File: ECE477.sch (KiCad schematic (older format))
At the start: 55 parts, among them IC1 LP3852EMP-3.3_NOPB, IC2 BQ29330DBT, J1 P7805-2000-S, J2 Conn_01x05_Male, J3 Conn_01x05_Male, J4 Conn_01x05_Male, J5 Conn_01x05_Male, J6 Conn_01x05_Male, SW1 SW_Push_Dual, U1 STM32H7_LQFP144_T2

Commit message: Updated Bat monitor
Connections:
- net GND: now also IC2.23 (VSS_2), IC2.4 (VSS_1); no longer IC2.1 (CELL-)
- net PWR_IN: now also IC2.19 (VCC); no longer IC2.2 (CELL+)
- net LED_PWR: now reaches IC2.24 (LEDOUT)
- net CLK: now reaches IC2.26 (WDI)
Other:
- moved on the sheet: IC2
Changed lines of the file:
@@
 Touch_Input
 Wire Wire Line
-	16100 2000 16450 2000
-Wire Wire Line
-	16100 2100 16450 2100
-Wire Wire Line
-	16100 2200 16450 2200
-Text GLabel 16450 2000 2    50   Input ~ 0
+	16650 2000 17000 2000
+Wire Wire Line
+	16650 2100 17000 2100
+Wire Wire Line
+	16650 2200 17000 2200
+Text GLabel 17000 2000 2    50   Input ~ 0
 I2C2_SMBA
-Text GLabel 16450 2100 2    50   Input ~ 0
+Text GLabel 17000 2100 2    50   Input ~ 0
 I2C2_SDA
-Text GLabel 16450 2200 2    50   Input ~ 0
+Text GLabel 17000 2200 2    50   Input ~ 0
 I2C2_SCL
 $Comp
 L ECE477-rescue:BQ29330DBT-SamacSys_Parts IC2
 U 1 1 5F7B6D95
-P 14800 2000
-F 0 "IC2" H 15450 2265 50  0000 C CNN
-F 1 "BQ29330DBT" H 15450 2174 50  0000 C CNN
-F 2 "SamacSys_Parts:SOP50P640X120-30N" H 25950 4500 50  0001 L CNN
-F 3 "http://www.ti.com/general/docs/suppproductinfo.tsp?distId=26&gotoUrl=http%3A%2F%2Fwww.ti.com%2Flit%2Fgpn%2Fbq29330" H 25950 4400 50  0001 L CNN
-F 4 "TEXAS INSTRUMENTS - BQ29330DBT. - Li-Ion Battery, Li-Pol Full Protector, 2/3/4 Series, I2C interface, 4.5 V to 28 V supply, TSSOP-30" H 25950 4300 50  0001 L CNN "Description"
-F 5 "1.2" H 25950 4200 50  0001 L CNN "Height"
-F 6 "595-BQ29330DBT" H 25950 4100 50  0001 L CNN "Mouser Part Number"
-F 7 "https://www.mouser.co.uk/ProductDetail/Texas-Instruments/BQ29330DBT?qs=YxwvVplHM%2FnxR6WOWVPfQQ%3D%3D" H 25950 4000 50  0001 L CNN "Mouser Price/Stock"
-F 8 "Texas Instruments" H 25950 3900 50  0001 L CNN "Manufacturer_Name"
-F 9 "BQ29330DBT" H 25950 3800 50  0001 L CNN "Manufacturer_Part_Number"
-	1    14800 2000
+P 15350 2000
+F 0 "IC2" H 16000 2265 50  0000 C CNN
+F 1 "BQ29330DBT" H 16000 2174 50  0000 C CNN
+F 2 "SamacSys_Parts:SOP50P640X120-30N" H 26500 4500 50  0001 L CNN
+F 3 "http://www.ti.com/general/docs/suppproductinfo.tsp?distId=26&gotoUrl=http%3A%2F%2Fwww.ti.com%2Flit%2Fgpn%2Fbq29330" H 26500 4400 50  0001 L CNN
+F 4 "TEXAS INSTRUMENTS - BQ29330DBT. - Li-Ion Battery, Li-Pol Full Protector, 2/3/4 Series, I2C interface, 4.5 V to 28 V supply, TSSOP-30" H 26500 4300 50  0001 L CNN "Description"
+F 5 "1.2" H 26500 4200 50  0001 L CNN "Height"
+F 6 "595-BQ29330DBT" H 26500 4100 50  0001 L CNN "Mouser Part Number"
+F 7 "https://www.mouser.co.uk/ProductDetail/Texas-Instruments/BQ29330DBT?qs=YxwvVplHM%2FnxR6WOWVPfQQ%3D%3D" H 26500 4000 50  0001 L CNN "Mouser Price/Stock"
+F 8 "Texas Instruments" H 26500 3900 50  0001 L CNN "Manufacturer_Name"
+F 9 "BQ29330DBT" H 26500 3800 50  0001 L CNN "Manufacturer_Part_Number"
+	1    15350 2000
 	1    0    0    -1
 $EndComp
@@
 Text GLabel 9700 3300 2    50   Input ~ 0
 PWM5
-Wire Wire Line
-	14800 2000 14500 2000
-Wire Wire Line
-	14800 2100 14500 2100
-Text GLabel 14500 2000 0    50   Input ~ 0
-GND
-Text GLabel 14500 2100 0    50   Input ~ 0
+Text GLabel 17000 3100 2    50   Input ~ 0
 PWR_IN
 Wire Wire Line
-	14800 3100 14450 3100
-Wire Wire Line
-	14800 3000 14450 3000
-Wire Wire Line
-	14800 2900 14450 2900
-Wire Wire Line
-	14800 2800 14450 2800
-Wire Wire Line
-	14800 2700 14450 2700
-Text GLabel 14450 2700 0    50   Input ~ 0
+	15350 3100 15000 3100
+Wire Wire Line
+	15350 3000 15000 3000
+Wire Wire Line
+	15350 2900 15000 2900
+Wire Wire Line
+	15350 2800 15000 2800
+Wire Wire Line
+	15350 2700 15000 2700
+Text GLabel 15000 2700 0    50   Input ~ 0
 V5
-Text GLabel 14450 2800 0    50   Input ~ 0
+Text GLabel 15000 2800 0    50   Input ~ 0
 V4
-Text GLabel 14450 2900 0    50   Input ~ 0
+Text GLabel 15000 2900 0    50   Input ~ 0
 V3
-Text GLabel 14450 3000 0    50   Input ~ 0
+Text GLabel 15000 3000 0    50   Input ~ 0
 V2
-Text GLabel 14450 3100 0    50   Input ~ 0
+Text GLabel 15000 3100 0    50   Input ~ 0
 V1
 Wire Notes Line
@@
 Text Notes 14800 4050 0    50   ~ 0
 review data sheet for PACK and BAT pions\n
-Wire Wire Line
-	16100 3300 16400 3300
-Text GLabel 16400 3300 2    50   Input ~ 0
+Text GLabel 17000 3300 2    50   Input ~ 0
 PWR_IN
-Wire Wire Line
-	14800 3200 14500 3200
-Text GLabel 14500 3200 0    50   Input ~ 0
+Text GLabel 15000 3200 0    50   Input ~ 0
 PWR_IN
+Wire Wire Line
+	15350 2300 15000 2300
+Wire Wire Line
+	16650 2700 17000 2700
+Wire Wire Line
+	15000 2100 15350 2100
+Wire Wire Line
+	15000 2000 15350 2000
+Text GLabel 15000 2300 0    50   Input ~ 0
+GND
+Text GLabel 17000 2700 2    50   Input ~ 0
+GND
+Wire Wire Line
+	16650 3100 17000 3100
+Wire Wire Line
+	16650 3300 17000 3300
+Wire Wire Line
+	15000 3200 15350 3200
+Wire Wire Line
+	16650 2600 17000 2600
+Text GLabel 17000 2600 2    50   Input ~ 0
+LED_PWR
+Wire Wire Line
+	16650 2400 17000 2400
+Text GLabel 17000 2400 2    50   Input ~ 0
+CLK
 $EndSCHEMATC

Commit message: Working with Routing
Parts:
- removed R5: 0R, Resistor_SMD:R_0805_2012Metric_Pad1.15x1.40mm_HandSolder, symbol Device:R_US
- added J7: Conn_01x05_Male, Connector_PinHeader_1.00mm:PinHeader_1x05_P1.00mm_Vertical, symbol Connector:Conn_01x05_Male
- added R10, R7, R8, R9: 0R, Resistor_SMD:R_0805_2012Metric_Pad1.15x1.40mm_HandSolder, symbol Device:R_US
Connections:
- net CLK is gone; now on net NC: IC2.26 (WDI)
- net LED_PWR is gone; now on net NC: IC2.24 (LEDOUT)
- net 1V2_MCU: now also R10.1, R9.2; no longer C23.1, C26.1, C27.1, L1.2, R11.1, U1.103 (VCAP), U1.140 (VCAP), U1.68 (VCAP)
- net 3V3_VDD: now also R8.1
- net BOOT0: now also R8.2
- net GND: now also R7.1; no longer C16.2, C17.2, C18.2, C19.2, U1.34 (VSSA)
- net NC: now reaches U1.10 (PC14-OSC32_IN)
- net NC: now also IC2.14 (CHG), IC2.15 (NC_1), IC2.16 (DSG), IC2.18 (NC_2), IC2.20 (ZVCHG), IC2.21 (GPOD), IC2.22 (PMS), IC2.25 (TOUT), IC2.27 (NC_3), IC2.3 (REG), IC2.5 (XRST), IC2.6 (SRN), IC2.7 (SRP), U1.1 (PE2), U1.100 (PA11), U1.101 (PA12), U1.11 (PC15-OSC32_OUT), U1.111 (PC12), U1.117 (PD5), U1.120 (PD6), U1.121 (PD7), U1.122 (PG9), U1.123 (PG10), U1.124 (PG11), U1.125 (PG12), U1.126 (PG13), U1.127 (PG14), U1.132 (PB5), U1.133 (PB6), U1.134 (PB7), U1.137 (PB9), U1.138 (PE0), U1.139 (PE1), U1.142 (PDR_ON), U1.2 (PE3), U1.20 (PF6), U1.21 (PF7), U1.22 (PF8), U1.23 (PF9), U1.24 (PF10), U1.25 (PH0-OSC_IN), U1.26 (PH1-OSC_OUT), U1.28 (PC0), U1.29 (PC1), U1.3 (PE4), U1.30 (PC2_C), U1.31 (PC3_C), U1.37 (PA0), U1.38 (PA1), U1.39 (PA2), U1.4 (PE5), U1.40 (PA3), U1.43 (PA4), U1.44 (PA5), U1.45 (PA6), U1.46 (PA7), U1.47 (PC4), U1.48 (PC5), U1.49 (PB0), U1.5 (PE6), U1.50 (PB1), U1.51 (PB2), U1.52 (PF11), U1.53 (PF14), U1.54 (PF15), U1.57 (PE7), U1.58 (PE8), U1.59 (PE9), U1.60 (PE10), U1.61 (PE11), U1.62 (PE12), U1.63 (PE13), U1.64 (PE14), U1.65 (PE15), U1.73 (PB13), U1.74 (PB14), U1.75 (PB15), U1.76 (PD8), U1.77 (PD9), U1.78 (PD10), U1.81 (PD11), U1.82 (PD12), U1.83 (PD13), U1.84 (PD14), U1.85 (PD15), U1.86 (PG6), U1.87 (PG7), U1.88 (PG8), U1.9 (PC13), U1.95 (PC8), U1.96 (PC9), U1.97 (PA8), J7.3 (Pin_3), J7.4 (Pin_4), J7.5 (Pin_5)
- net CELL-: now reaches IC2.1 (CELL-)
- net CELL-: now also J7.1 (Pin_1)
- net CELL+: now reaches IC2.2 (CELL+)
- net CELL+: now also J7.2 (Pin_2)
- net 3.3V renamed 3.3_VDD
- new net GNDA: C16.2, C17.2, C18.2, C19.2, R7.2, U1.34 (VSSA)
- new net VCAP: C26.1, C27.1, R10.2, R11.1, U1.103 (VCAP), U1.140 (VCAP), U1.68 (VCAP)
- new net VDD_SMPS_IND_OUT: C23.1, L1.2, R9.1
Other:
- note added: "Bat - Monitor Connections V2\n"
- note added: "WDI goes to CLK and LEDOUT goes to LEDPWR\n"

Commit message: Finshed Routing One
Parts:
- removed C24, C25: 100nF, Capacitor_SMD:C_0805_2012Metric_Pad1.15x1.40mm_HandSolder, symbol pspice:CAP
- removed R9: 0R, Resistor_SMD:R_0805_2012Metric_Pad1.15x1.40mm_HandSolder, symbol Device:R_US
- added R14, R5: 0R, Resistor_SMD:R_0805_2012Metric_Pad1.15x1.40mm_HandSolder, symbol Device:R_US
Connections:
- net 3.3_VDD is gone; now on net 3V3_VDD: J5.2 (Pin_2)
- net VBAT: now also R5.1; no longer C1.1, C10.1, C11.1, C12.1, C13.1, C14.1, C2.1, C20.1, C21.1, C3.1, C4.1, C5.1, C6.1, C7.1, C8.1, C9.1, JP1.2 (C), R1.1, R3.2, U1.106 (VDD), U1.119 (VDD), U1.129 (VDD), U1.13 (VDD), U1.144 (VDD), U1.16 (VDDSMPS), U1.19 (VDD), U1.32 (VDD), U1.42 (VDD), U1.56 (VDD), U1.7 (VDD), U1.71 (VDD), U1.79 (VDD), U1.92 (VDD)
- net VDD_LDO: now also R10.1
- net VDD_SMPS_IND_OUT: now also R6.1
- removed net 1V2_MCU: R10.1, R6.1
- removed net NC: IC2.14 (CHG), IC2.15 (NC_1), IC2.16 (DSG), IC2.18 (NC_2), IC2.20 (ZVCHG), IC2.21 (GPOD), IC2.22 (PMS), IC2.24 (LEDOUT), IC2.25 (TOUT), IC2.26 (WDI), IC2.27 (NC_3), IC2.3 (REG), IC2.5 (XRST), IC2.6 (SRN), IC2.7 (SRP), J7.3 (Pin_3), J7.4 (Pin_4), J7.5 (Pin_5), U1.1 (PE2), U1.10 (PC14-OSC32_IN), U1.100 (PA11), U1.101 (PA12), U1.11 (PC15-OSC32_OUT), U1.111 (PC12), U1.117 (PD5), U1.120 (PD6), U1.121 (PD7), U1.122 (PG9), U1.123 (PG10), U1.124 (PG11), U1.125 (PG12), U1.126 (PG13), U1.127 (PG14), U1.132 (PB5), U1.133 (PB6), U1.134 (PB7), U1.137 (PB9), U1.138 (PE0), U1.139 (PE1), U1.142 (PDR_ON), U1.2 (PE3), U1.20 (PF6), U1.21 (PF7), U1.22 (PF8), U1.23 (PF9), U1.24 (PF10), U1.25 (PH0-OSC_IN), U1.26 (PH1-OSC_OUT), U1.28 (PC0), U1.29 (PC1), U1.3 (PE4), U1.30 (PC2_C), U1.31 (PC3_C), U1.37 (PA0), U1.38 (PA1), U1.39 (PA2), U1.4 (PE5), U1.40 (PA3), U1.43 (PA4), U1.44 (PA5), U1.45 (PA6), U1.46 (PA7), U1.47 (PC4), U1.48 (PC5), U1.49 (PB0), U1.5 (PE6), U1.50 (PB1), U1.51 (PB2), U1.52 (PF11), U1.53 (PF14), U1.54 (PF15), U1.57 (PE7), U1.58 (PE8), U1.59 (PE9), U1.60 (PE10), U1.61 (PE11), U1.62 (PE12), U1.63 (PE13), U1.64 (PE14), U1.65 (PE15), U1.73 (PB13), U1.74 (PB14), U1.75 (PB15), U1.76 (PD8), U1.77 (PD9), U1.78 (PD10), U1.81 (PD11), U1.82 (PD12), U1.83 (PD13), U1.84 (PD14), U1.85 (PD15), U1.86 (PG6), U1.87 (PG7), U1.88 (PG8), U1.9 (PC13), U1.95 (PC8), U1.96 (PC9), U1.97 (PA8)
- new net VDDSMPS_IN: C20.1, C21.1, R14.2, U1.16 (VDDSMPS)
- new net VDD_MCU: C1.1, C10.1, C11.1, C12.1, C13.1, C14.1, C2.1, C3.1, C4.1, C5.1, C6.1, C7.1, C8.1, C9.1, JP1.2 (C), R1.1, R14.1, R3.2, R5.2, U1.106 (VDD), U1.119 (VDD), U1.129 (VDD), U1.13 (VDD), U1.144 (VDD), U1.19 (VDD), U1.32 (VDD), U1.42 (VDD), U1.56 (VDD), U1.7 (VDD), U1.71 (VDD), U1.79 (VDD), U1.92 (VDD)
- no-connect marks 0 -> 98
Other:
- note removed: "Must be place near VDD_LDO\n"
- note removed: "Must be used if using LDO pwr supply"

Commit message: review with team
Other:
- note removed: "review data sheet for PACK and BAT pions\n"
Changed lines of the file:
@@
 	0    1    1    0
 $EndComp
-Text Notes 14800 4050 0    50   ~ 0
-review data sheet for PACK and BAT pions\n
 Text GLabel 17000 3300 2    50   Input ~ 0
 PWR_IN

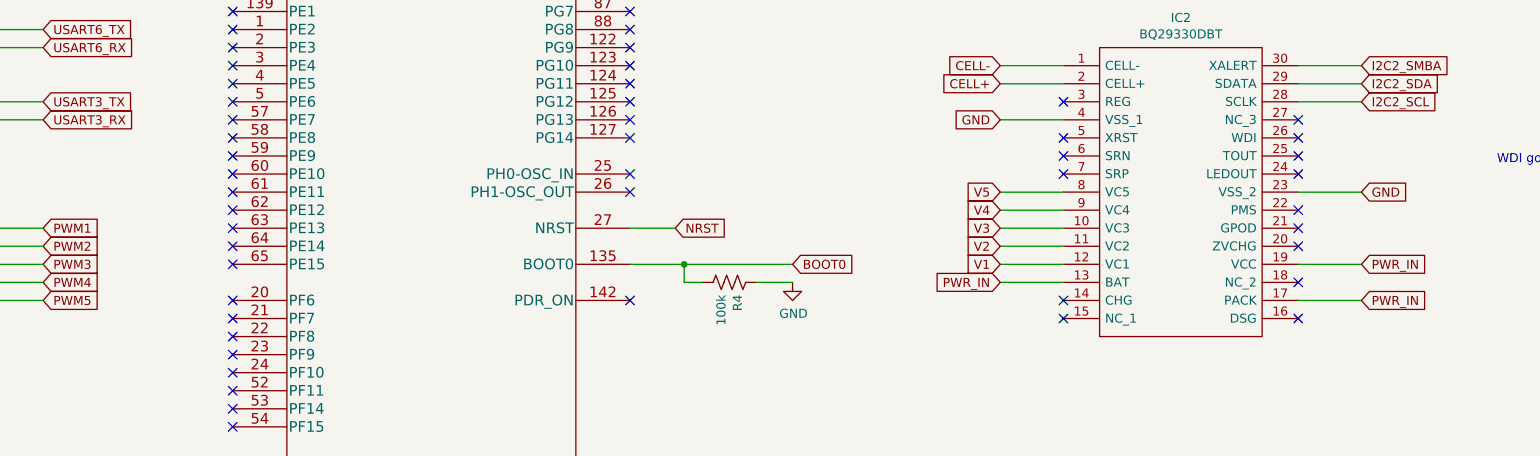
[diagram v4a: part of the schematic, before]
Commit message: Updated CLK for Bq29330DBT
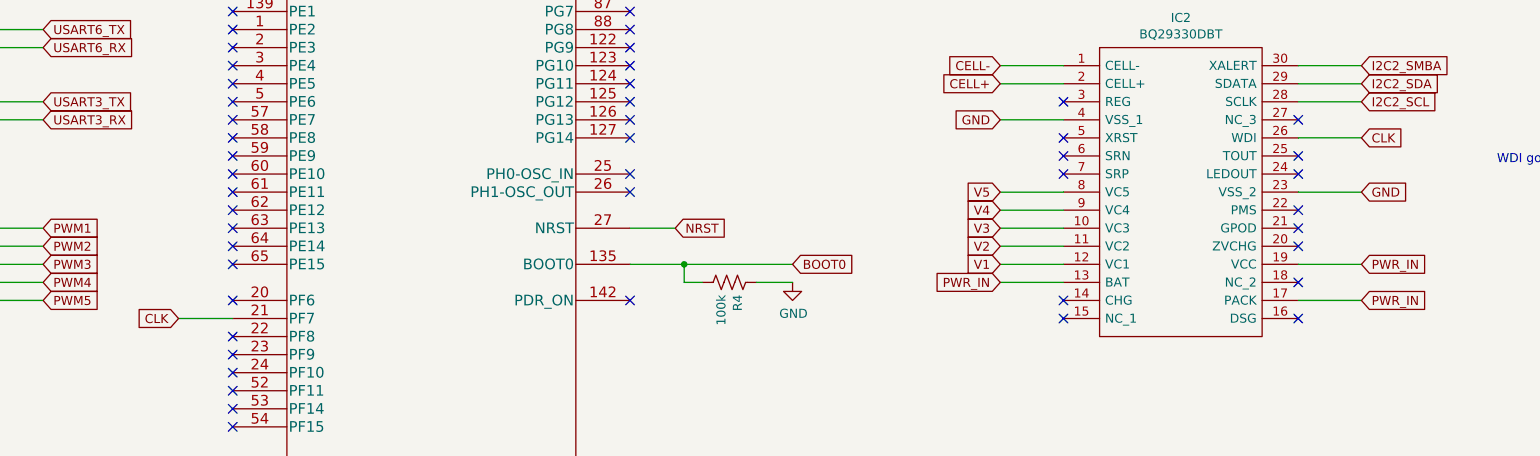
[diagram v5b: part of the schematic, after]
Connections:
- net CLK: now reaches U1.21 (PF7)
- net CLK: now also IC2.26 (WDI)
- no-connect marks 98 -> 96
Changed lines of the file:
@@
 Connection ~ 2650 13250
 NoConn ~ 16650 2300
-NoConn ~ 16650 2400
 NoConn ~ 16650 2500
 NoConn ~ 16650 2600
@@
 NoConn ~ 10750 3600
 NoConn ~ 10750 3500
-NoConn ~ 10750 3400
 NoConn ~ 10750 3300
 NoConn ~ 10750 3100
@@
 Text GLabel 4600 8800 1    50   Input ~ 0
 VDD_LDO
+Wire Wire Line
+	10750 3400 10450 3400
+Text GLabel 10450 3400 0    50   Input ~ 0
+CLK
+Text GLabel 17000 2400 2    50   Input ~ 0
+CLK
+Wire Wire Line
+	16650 2400 17000 2400
 $EndSCHEMATC

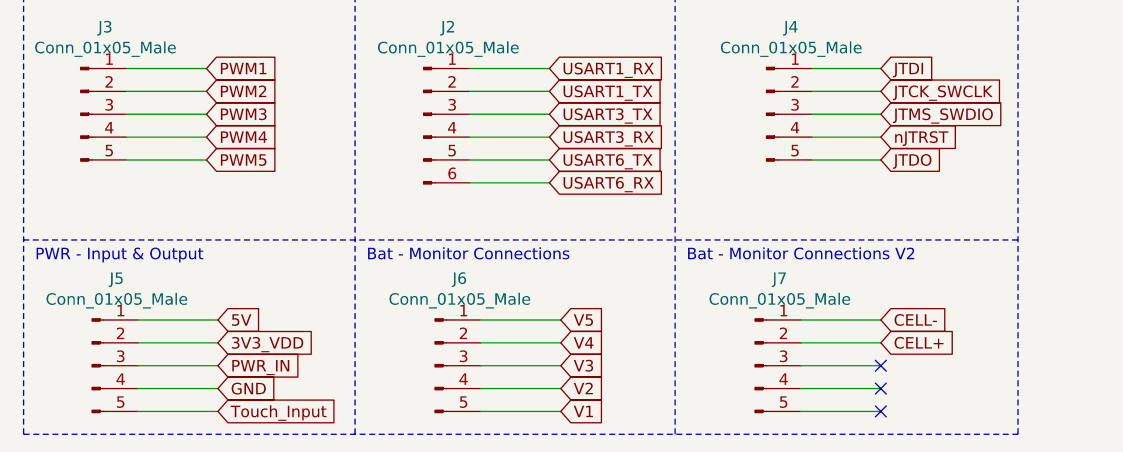
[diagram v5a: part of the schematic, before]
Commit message: Updates #1 post meeting with TODD
Updated pins and added GNDs for serial communication refreces.
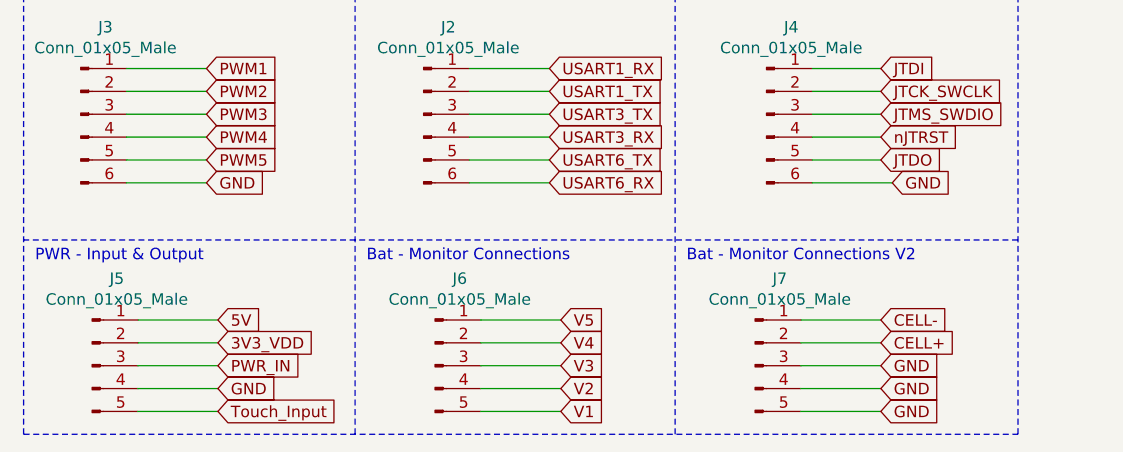
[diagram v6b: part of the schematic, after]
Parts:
- removed J3, J4: Conn_01x05_Male, Connector_PinHeader_1.00mm:PinHeader_1x05_P1.00mm_Vertical, symbol Connector:Conn_01x05_Male
- added J3, J4: Conn_01x05_Male, Connector_PinHeader_2.54mm:PinHeader_1x06_P2.54mm_Vertical, symbol Connector:Conn_01x06_Male
- J2: footprint Connector_PinHeader_1.00mm:PinHeader_1x06_P1.00mm_Vertical -> Connector_PinHeader_2.54mm:PinHeader_1x06_P2.54mm_Vertical
- J5, J6, J7: footprint Connector_PinHeader_1.00mm:PinHeader_1x05_P1.00mm_Vertical -> Connector_PinHeader_2.54mm:PinHeader_1x05_P2.54mm_Vertical
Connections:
- net GND: now also J7.3 (Pin_3), J7.4 (Pin_4), J7.5 (Pin_5), J3.6 (Pin_6), J4.6 (Pin_6)
- net JTCK_SWCLK: now also J4.2 (Pin_2)
- net JTDI: now also J4.1 (Pin_1)
- net JTDO: now also J4.5 (Pin_5)
- net JTMS_SWDIO: now also J4.3 (Pin_3)
- net PWM1: now also J3.1 (Pin_1)
- net PWM2: now also J3.2 (Pin_2)
- net PWM3: now also J3.3 (Pin_3)
- net PWM4: now also J3.4 (Pin_4)
- net PWM5: now also J3.5 (Pin_5)
- net nJTRST: now also J4.4 (Pin_4)
- no-connect marks 96 -> 93
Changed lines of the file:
@@
 Wire Wire Line
 	2550 15750 2900 15750
-$Comp
-L Connector:Conn_01x05_Male J6
-U 1 1 5F8FE391
-P 2350 15950
-F 0 "J6" H 2458 16331 50  0000 C CNN
-F 1 "Conn_01x05_Male" H 2458 16240 50  0000 C CNN
-F 2 "Connector_PinHeader_1.00mm:PinHeader_1x05_P1.00mm_Vertical" H 2350 15950 50  0001 C CNN
-F 3 "~" H 2350 15950 50  0001 C CNN
-	1    2350 15950
-	1    0    0    -1
-$EndComp
 Text Notes 600  15500 0    50   ~ 0
 PWR - Input & Output\n
@@
 F 0 "J5" H 958 16331 50  0000 C CNN
 F 1 "Conn_01x05_Male" H 958 16240 50  0000 C CNN
-F 2 "Connector_PinHeader_1.00mm:PinHeader_1x05_P1.00mm_Vertical" H 850 15950 50  0001 C CNN
+F 2 "Connector_PinHeader_2.54mm:PinHeader_1x05_P2.54mm_Vertical" H 850 15950 50  0001 C CNN
 F 3 "~" H 850 15950 50  0001 C CNN
 	1    850  15950
@@
 	2500 14650 2850 14650
 $Comp
-L Connector:Conn_01x05_Male J3
-U 1 1 5FA398AC
-P 800 14850
-F 0 "J3" H 908 15231 50  0000 C CNN
-F 1 "Conn_01x05_Male" H 908 15140 50  0000 C CNN
-F 2 "Connector_PinHeader_1.00mm:PinHeader_1x05_P1.00mm_Vertical" H 800 14850 50  0001 C CNN
-F 3 "~" H 800 14850 50  0001 C CNN
-	1    800  14850
-	1    0    0    -1
-$EndComp
-$Comp
-L Connector:Conn_01x05_Male J4
-U 1 1 5FA2B098
-P 3800 14850
-F 0 "J4" H 3908 15231 50  0000 C CNN
-F 1 "Conn_01x05_Male" H 3908 15140 50  0000 C CNN
-F 2 "Connector_PinHeader_1.00mm:PinHeader_1x05_P1.00mm_Vertical" H 3800 14850 50  0001 C CNN
-F 3 "~" H 3800 14850 50  0001 C CNN
-	1    3800 14850
-	1    0    0    -1
-$EndComp
-$Comp
 L Connector:Conn_01x06_Male J2
 U 1 1 5FA28754
@@
 F 0 "J2" H 2408 15231 50  0000 C CNN
 F 1 "Conn_01x05_Male" H 2408 15140 50  0000 C CNN
-F 2 "Connector_PinHeader_1.00mm:PinHeader_1x06_P1.00mm_Vertical" H 2300 14850 50  0001 C CNN
+F 2 "Connector_PinHeader_2.54mm:PinHeader_1x06_P2.54mm_Vertical" H 2300 14850 50  0001 C CNN
 F 3 "~" H 2300 14850 50  0001 C CNN
 	1    2300 14850
@@
 	15000 3200 15350 3200
 Wire Wire Line
-	3950 16150 4300 16150
-Wire Wire Line
-	3950 16050 4300 16050
-Wire Wire Line
-	3950 15950 4300 15950
-Wire Wire Line
 	3950 15850 4300 15850
 Wire Wire Line
@@
 F 0 "J7" H 3858 16331 50  0000 C CNN
 F 1 "Conn_01x05_Male" H 3858 16240 50  0000 C CNN
-F 2 "Connector_PinHeader_1.00mm:PinHeader_1x05_P1.00mm_Vertical" H 3750 15950 50  0001 C CNN
+F 2 "Connector_PinHeader_2.54mm:PinHeader_1x05_P2.54mm_Vertical" H 3750 15950 50  0001 C CNN
 F 3 "~" H 3750 15950 50  0001 C CNN
 	1    3750 15950
@@
 NoConn ~ 6950 4300
 NoConn ~ 6950 4400
-NoConn ~ 4300 15950
-NoConn ~ 4300 16050
-NoConn ~ 4300 16150
 $Comp
 L Device:R_US R5
@@
 Wire Wire Line
 	16650 2400 17000 2400
+$Comp
+L Connector:Conn_01x06_Male J3
+U 1 1 5F8B51CF
+P 800 14850
+F 0 "J3" H 908 15231 50  0000 C CNN
+F 1 "Conn_01x05_Male" H 908 15140 50  0000 C CNN
+F 2 "Connector_PinHeader_2.54mm:PinHeader_1x06_P2.54mm_Vertical" H 800 14850 50  0001 C CNN
+F 3 "~" H 800 14850 50  0001 C CNN
+	1    800  14850
+	1    0    0    -1
+$EndComp
+$Comp
+L Connector:Conn_01x06_Male J4
+U 1 1 5F8E70FD
+P 3800 14850
+F 0 "J4" H 3908 15231 50  0000 C CNN
+F 1 "Conn_01x05_Male" H 3908 15140 50  0000 C CNN
+F 2 "Connector_PinHeader_2.54mm:PinHeader_1x06_P2.54mm_Vertical" H 3800 14850 50  0001 C CNN
+F 3 "~" H 3800 14850 50  0001 C CNN
+	1    3800 14850
+	1    0    0    -1
+$EndComp
+$Comp
+L Connector:Conn_01x05_Male J6
+U 1 1 5F8FE391
+P 2350 15950
+F 0 "J6" H 2458 16331 50  0000 C CNN
+F 1 "Conn_01x05_Male" H 2458 16240 50  0000 C CNN
+F 2 "Connector_PinHeader_2.54mm:PinHeader_1x05_P2.54mm_Vertical" H 2350 15950 50  0001 C CNN
+F 3 "~" H 2350 15950 50  0001 C CNN
+	1    2350 15950
+	1    0    0    -1
+$EndComp
+Text GLabel 1350 15150 2    50   Input ~ 0
+GND
+Wire Wire Line
+	1000 15150 1350 15150
+Text GLabel 4350 15150 2    50   Input ~ 0
+GND
+Wire Wire Line
+	4000 15150 4350 15150
+Text GLabel 4300 16150 2    50   Input ~ 0
+GND
+Wire Wire Line
+	3950 16150 4300 16150
+Text GLabel 4300 16050 2    50   Input ~ 0
+GND
+Wire Wire Line
+	3950 16050 4300 16050
+Text GLabel 4300 15950 2    50   Input ~ 0
+GND
+Wire Wire Line
+	3950 15950 4300 15950
 $EndSCHEMATC

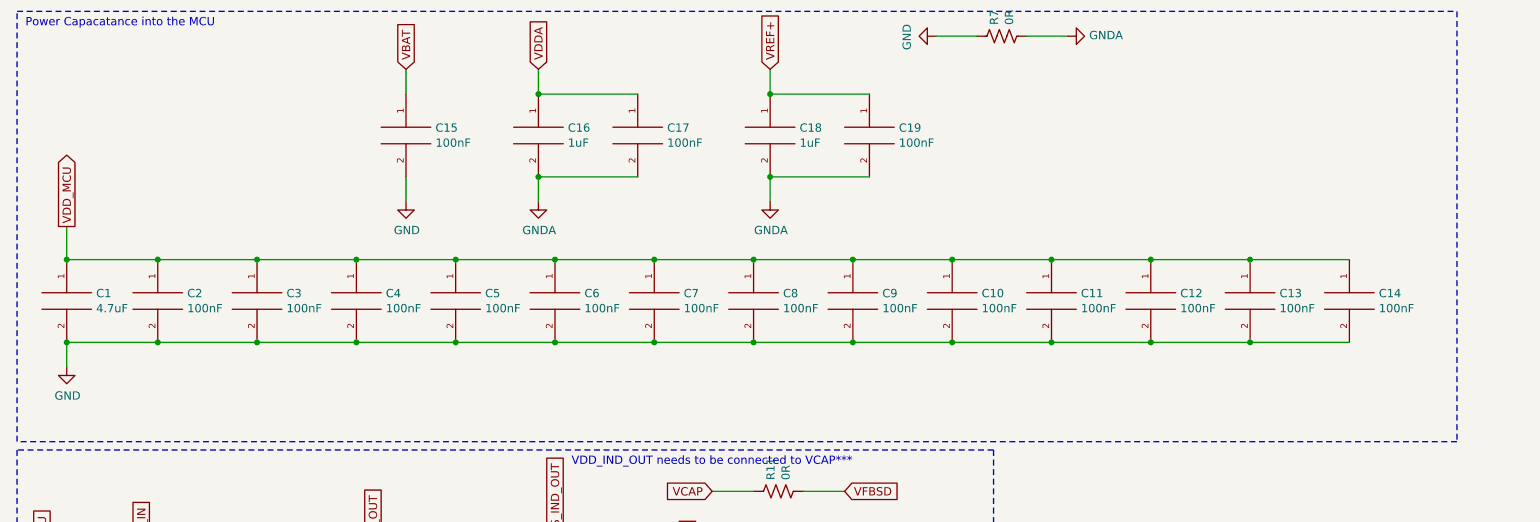
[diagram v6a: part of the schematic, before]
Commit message: Updated with single cap
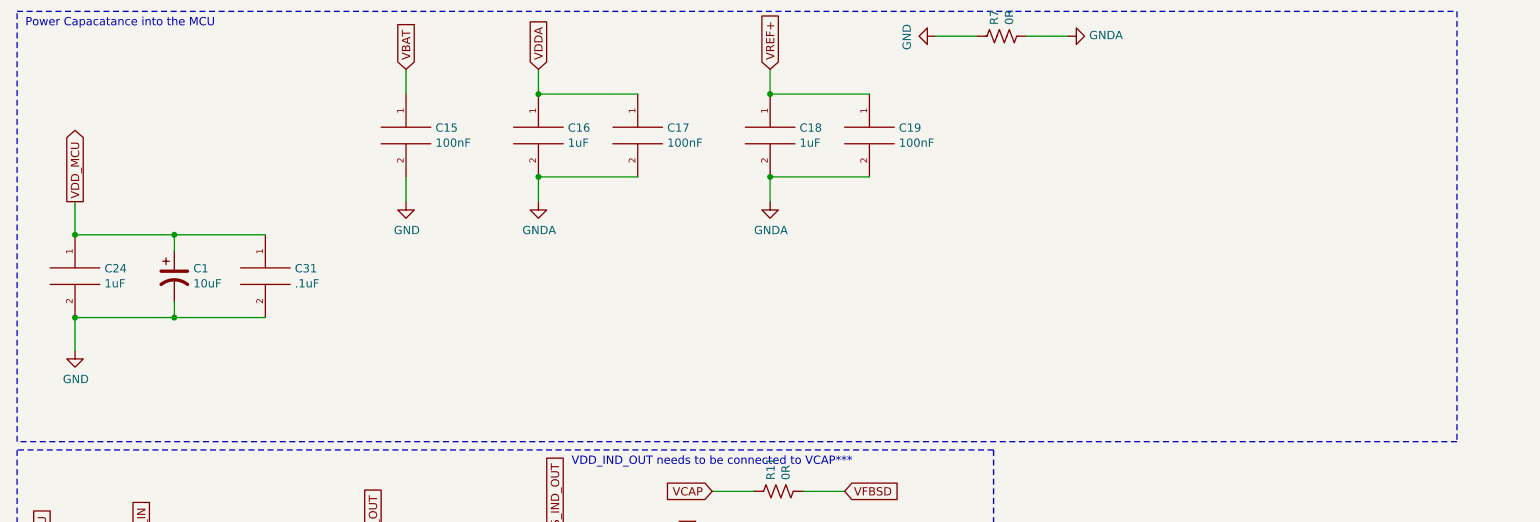
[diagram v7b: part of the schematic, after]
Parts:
- removed C1: 4.7uF, Capacitor_SMD:C_0805_2012Metric_Pad1.15x1.40mm_HandSolder, symbol pspice:CAP
- removed C10, C11, C12, C13, C14, C2, C3, C4, C5, C6, C7, C8, C9: 100nF, Capacitor_SMD:C_0805_2012Metric_Pad1.15x1.40mm_HandSolder, symbol pspice:CAP
- added C1: 10uF, Capacitor_THT:CP_Radial_D5.0mm_P2.50mm, symbol Device:CP1
- added C24: 1uF, Capacitor_SMD:C_0805_2012Metric_Pad1.15x1.40mm_HandSolder, symbol pspice:CAP
- added C31: .1uF, Capacitor_SMD:C_0805_2012Metric_Pad1.15x1.40mm_HandSolder, symbol pspice:CAP
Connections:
- net GND: now also C1.2, C24.2, C31.2
- net VDD_MCU: now also C1.1, C24.1, C31.1
